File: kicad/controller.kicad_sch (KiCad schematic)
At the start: 28 parts, among them J6 USB_B_Micro, J7 PROG, Q3 SS8050-G, Q4 SS8050-G, U5 CP2102N-A02-GQFN24, U6 ESP32-WROOM-32E

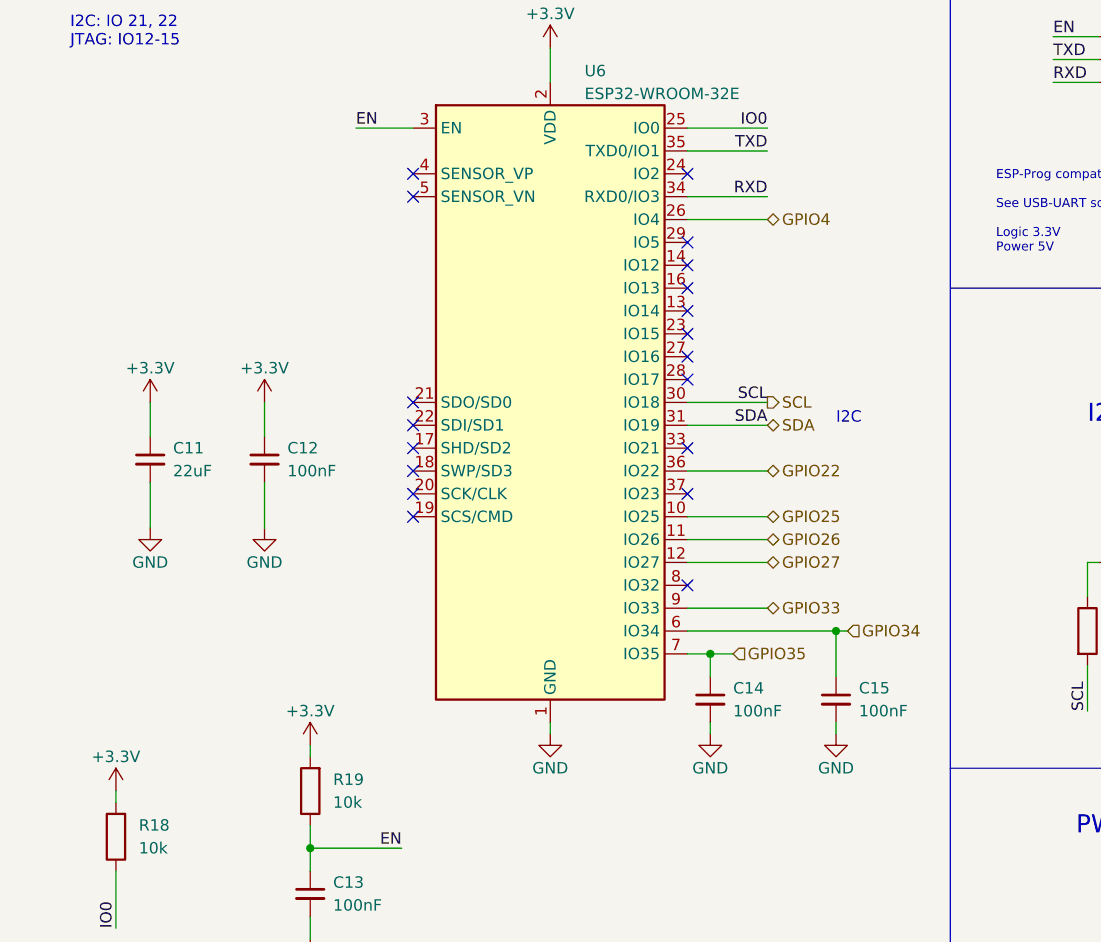
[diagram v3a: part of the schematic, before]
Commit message: use sensor_vp/vn for ADC
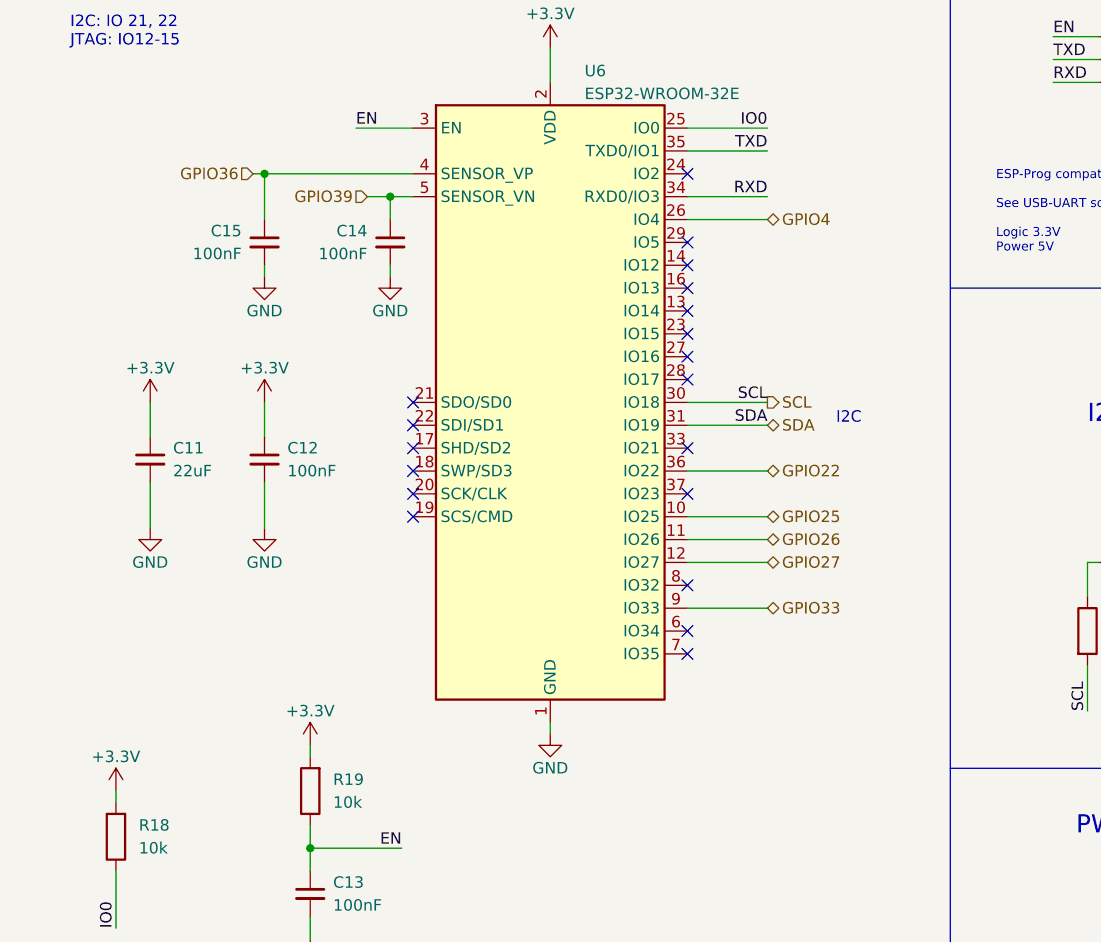
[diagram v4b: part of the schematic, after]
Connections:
- net GPIO36: now reaches U6.4 (SENSOR_VP)
- net GPIO36: now also C15.1
- net GPIO39: now reaches U6.5 (SENSOR_VN)
- net GPIO39: now also C14.1
- net GPIO34: no longer names the net of U6.6 (IO34)
- net GPIO34: no longer C15.1
- net GPIO35: no longer names the net of U6.7 (IO35)
- net GPIO35: no longer C14.1
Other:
- moved on the sheet: C14, C15
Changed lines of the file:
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@@
   (junction (at 74.93 71.12) (diameter 0) (color 0 0 0 0)
   )
-  (junction (at 214.63 107.95) (diameter 0) (color 0 0 0 0)
+  (junction (at 179.07 57.15) (diameter 0) (color 0 0 0 0)
   )
   (junction (at 83.82 165.1) (diameter 0) (color 0 0 0 0)
@@
   (junction (at 99.06 50.8) (diameter 0) (color 0 0 0 0)
   )
-  (junction (at 228.6 105.41) (diameter 0) (color 0 0 0 0)
+  (junction (at 165.1 54.61) (diameter 0) (color 0 0 0 0)
   )
   (junction (at 87.63 44.45) (diameter 0) (color 0 0 0 0)
@@
   (no_connect (at 114.3 76.2))
   (no_connect (at 181.61 87.63))
+  (no_connect (at 212.09 105.41))
+  (no_connect (at 212.09 107.95))
   (no_connect (at 212.09 69.85))
   (no_connect (at 181.61 92.71))
@@
   (no_connect (at 114.3 91.44))
   (no_connect (at 114.3 73.66))
-  (no_connect (at 181.61 54.61))
   (no_connect (at 212.09 90.17))
   (no_connect (at 181.61 80.01))
-  (no_connect (at 181.61 57.15))
   (no_connect (at 212.09 74.93))
   (no_connect (at 212.09 77.47))
@@
     (stroke (width 0) (type default) (color 0 0 0 0))
   )
-  (wire (pts (xy 214.63 115.57) (xy 214.63 116.84))
+  (wire (pts (xy 179.07 64.77) (xy 179.07 66.04))
     (stroke (width 0) (type default) (color 0 0 0 0))
   )
@@
     (stroke (width 0) (type default) (color 0 0 0 0))
   )
-  (wire (pts (xy 212.09 105.41) (xy 228.6 105.41))
+  (wire (pts (xy 181.61 54.61) (xy 165.1 54.61))
     (stroke (width 0) (type default) (color 0 0 0 0))
   )
@@
     (stroke (width 0) (type default) (color 0 0 0 0))
   )
-  (wire (pts (xy 214.63 107.95) (xy 212.09 107.95))
+  (wire (pts (xy 179.07 57.15) (xy 181.61 57.15))
     (stroke (width 0) (type default) (color 0 0 0 0))
   )
@@
     (stroke (width 0) (type default) (color 0 0 0 0))
   )
-  (wire (pts (xy 228.6 105.41) (xy 229.87 105.41))
+  (wire (pts (xy 165.1 54.61) (xy 163.83 54.61))
     (stroke (width 0) (type default) (color 0 0 0 0))
   )
@@
     (stroke (width 0) (type default) (color 0 0 0 0))
   )
-  (wire (pts (xy 228.6 115.57) (xy 228.6 116.84))
+  (wire (pts (xy 165.1 64.77) (xy 165.1 66.04))
     (stroke (width 0) (type default) (color 0 0 0 0))
   )
@@
     (stroke (width 0) (type default) (color 0 0 0 0))
   )
-  (wire (pts (xy 217.17 107.95) (xy 214.63 107.95))
+  (wire (pts (xy 176.53 57.15) (xy 179.07 57.15))
     (stroke (width 0) (type default) (color 0 0 0 0))
   )
@@
     (stroke (width 0) (type default) (color 0 0 0 0))
   )
-  (wire (pts (xy 228.6 105.41) (xy 228.6 110.49))
+  (wire (pts (xy 165.1 54.61) (xy 165.1 59.69))
     (stroke (width 0) (type default) (color 0 0 0 0))
   )
@@
     (stroke (width 0) (type default) (color 0 0 0 0))
   )
-  (wire (pts (xy 214.63 107.95) (xy 214.63 110.49))
+  (wire (pts (xy 179.07 57.15) (xy 179.07 59.69))
     (stroke (width 0) (type default) (color 0 0 0 0))
   )
@@
     (effects (font (size 1.27 1.27)) (justify left bottom))
   )
-  (hierarchical_label "GPIO34" (shape input) (at 229.87 105.41 0)
-    (effects (font (size 1.27 1.27)) (justify left))
+  (hierarchical_label "GPIO36" (shape input) (at 163.83 54.61 180)
+    (effects (font (size 1.27 1.27)) (justify right))
   )
   (hierarchical_label "GPIO26" (shape bidirectional) (at 220.98 95.25 0)
@@
     (effects (font (size 1.27 1.27)) (justify left))
   )
-  (hierarchical_label "GPIO35" (shape input) (at 217.17 107.95 0)
-    (effects (font (size 1.27 1.27)) (justify left))
+  (hierarchical_label "GPIO39" (shape input) (at 176.53 57.15 180)
+    (effects (font (size 1.27 1.27)) (justify right))
   )
   (hierarchical_label "GPIO22" (shape bidirectional) (at 220.98 87.63 0)
@@
     (pin "2")
   )
-  (symbol (lib_id "Device:C_Small") (at 228.6 113.03 0) (unit 1)
-    (in_bom yes) (on_board yes)
-    (property "Reference" "C15" (id 0) (at 231.14 111.76 0)
-      (effects (font (size 1.27 1.27)) (justify left))
-    )
-    (property "Value" "100nF" (id 1) (at 231.14 114.3 0)
-      (effects (font (size 1.27 1.27)) (justify left))
-    )
-    (property "Footprint" "Capacitor_SMD:C_0603_1608Metric" (id 2) (at 228.6 113.03 0)
-      (effects (font (size 1.27 1.27)) hide)
-    )
-    (property "Datasheet" "~" (id 3) (at 228.6 113.03 0)
-      (effects (font (size 1.27 1.27)) hide)
-    )
-    (property "MPN" "CL10B104KB8NNWC" (id 4) (at 228.6 113.03 0)
-      (effects (font (size 1.27 1.27)) hide)
-    )
-    (property "LCSC" "C1591" (id 5) (at 228.6 113.03 0)
-      (effects (font (size 1.27 1.27)) hide)
-    )
-    (property "MOUSER" "187-CL10B104KB8NNNC" (id 6) (at 228.6 113.03 0)
+  (symbol (lib_id "Device:C_Small") (at 165.1 62.23 0) (mirror y) (unit 1)
+    (in_bom yes) (on_board yes)
+    (property "Reference" "C15" (id 0) (at 162.56 60.96 0)
+      (effects (font (size 1.27 1.27)) (justify left))
+    )
+    (property "Value" "100nF" (id 1) (at 162.56 63.5 0)
+      (effects (font (size 1.27 1.27)) (justify left))
+    )
+    (property "Footprint" "Capacitor_SMD:C_0603_1608Metric" (id 2) (at 165.1 62.23 0)
+      (effects (font (size 1.27 1.27)) hide)
+    )
+    (property "Datasheet" "~" (id 3) (at 165.1 62.23 0)
+      (effects (font (size 1.27 1.27)) hide)
+    )
+    (property "MPN" "CL10B104KB8NNWC" (id 4) (at 165.1 62.23 0)
+      (effects (font (size 1.27 1.27)) hide)
+    )
+    (property "LCSC" "C1591" (id 5) (at 165.1 62.23 0)
+      (effects (font (size 1.27 1.27)) hide)
+    )
+    (property "MOUSER" "187-CL10B104KB8NNNC" (id 6) (at 165.1 62.23 0)
       (effects (font (size 1.27 1.27)) hide)
     )
@@
     (pin "1")
   )
-  (symbol (lib_id "Device:C_Small") (at 214.63 113.03 0) (mirror y) (unit 1)
+  (symbol (lib_id "Device:C_Small") (at 179.07 62.23 0) (unit 1)
     (in_bom yes) (on_board yes) (fields_autoplaced)
-    (property "Reference" "C14" (id 0) (at 217.17 111.7662 0)
+    (property "Reference" "C14" (id 0) (at 176.53 60.9662 0)
       (effects (font (size 1.27 1.27)) (justify right))
     )
-    (property "Value" "100nF" (id 1) (at 217.17 114.3062 0)
+    (property "Value" "100nF" (id 1) (at 176.53 63.5062 0)
       (effects (font (size 1.27 1.27)) (justify right))
     )
-    (property "Footprint" "Capacitor_SMD:C_0603_1608Metric" (id 2) (at 214.63 113.03 0)
-      (effects (font (size 1.27 1.27)) hide)
-    )
-    (property "Datasheet" "~" (id 3) (at 214.63 113.03 0)
-      (effects (font (size 1.27 1.27)) hide)
-    )
-    (property "MPN" "CL10B104KB8NNWC" (id 4) (at 214.63 113.03 0)
-      (effects (font (size 1.27 1.27)) hide)
-    )
-    (property "LCSC" "C1591" (id 5) (at 214.63 113.03 0)
-      (effects (font (size 1.27 1.27)) hide)
-    )
-    (property "MOUSER" "187-CL10B104KB8NNNC" (id 6) (at 214.63 113.03 0)
+    (property "Footprint" "Capacitor_SMD:C_0603_1608Metric" (id 2) (at 179.07 62.23 0)
+      (effects (font (size 1.27 1.27)) hide)
+    )
+    (property "Datasheet" "~" (id 3) (at 179.07 62.23 0)
+      (effects (font (size 1.27 1.27)) hide)
+    )
+    (property "MPN" "CL10B104KB8NNWC" (id 4) (at 179.07 62.23 0)
+      (effects (font (size 1.27 1.27)) hide)
+    )
+    (property "LCSC" "C1591" (id 5) (at 179.07 62.23 0)
+      (effects (font (size 1.27 1.27)) hide)
+    )
+    (property "MOUSER" "187-CL10B104KB8NNNC" (id 6) (at 179.07 62.23 0)
       (effects (font (size 1.27 1.27)) hide)
     )
@@
     (pin "1")
   )
-  (symbol (lib_id "power:GND") (at 228.6 116.84 0) (mirror y) (unit 1)
-    (in_bom yes) (on_board yes)
-    (property "Reference" "#PWR065" (id 0) (at 228.6 123.19 0)
-      (effects (font (size 1.27 1.27)) hide)
-    )
-    (property "Value" "GND" (id 1) (at 228.6 120.65 0))
-    (property "Footprint" "" (id 2) (at 228.6 116.84 0)
-      (effects (font (size 1.27 1.27)) hide)
-    )
-    (property "Datasheet" "" (id 3) (at 228.6 116.84 0)
+  (symbol (lib_id "power:GND") (at 165.1 66.04 0) (unit 1)
+    (in_bom yes) (on_board yes)
+    (property "Reference" "#PWR065" (id 0) (at 165.1 72.39 0)
+      (effects (font (size 1.27 1.27)) hide)
+    )
+    (property "Value" "GND" (id 1) (at 165.1 69.85 0))
+    (property "Footprint" "" (id 2) (at 165.1 66.04 0)
+      (effects (font (size 1.27 1.27)) hide)
+    )
+    (property "Datasheet" "" (id 3) (at 165.1 66.04 0)
       (effects (font (size 1.27 1.27)) hide)
     )
@@
     (pin "1")
   )
-  (symbol (lib_id "power:GND") (at 214.63 116.84 0) (mirror y) (unit 1)
-    (in_bom yes) (on_board yes)
-    (property "Reference" "#PWR064" (id 0) (at 214.63 123.19 0)
-      (effects (font (size 1.27 1.27)) hide)
-    )
-    (property "Value" "GND" (id 1) (at 214.63 120.65 0))
-    (property "Footprint" "" (id 2) (at 214.63 116.84 0)
-      (effects (font (size 1.27 1.27)) hide)
-    )
-    (property "Datasheet" "" (id 3) (at 214.63 116.84 0)
-      (effects (font (size 1.27 1.27)) hide)
-    )
+  (symbol (lib_id "power:GND") (at 179.07 66.04 0) (unit 1)
+    (in_bom yes) (on_board yes)
+    (property "Reference" "#PWR064" (id 0) (at 179.07 72.39 0)
+      (effects (font (size 1.27 1.27)) hide)
+    )
+    (property "Value" "GND" (id 1) (at 179.07 69.85 0))
+    (property "Footprint" "" (id 2) (at 179.07 66.04 0)
+      (effects (font (size 1.27 1.27)) hide)
+    )
+    (property "Datasheet" "" (id 3) (at 179.07 66.04 0)
+      (effects (font (size 1.27 1.27)) hide)
+    )
